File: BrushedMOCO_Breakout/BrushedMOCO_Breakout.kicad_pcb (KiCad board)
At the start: 2 copper layers, 39.9 x 46.2 mm, 30 parts, among them Q1 Si4156DY, Q2 Si4156DY, Q3 Si4156DY, Q4 Si4156DY, U1 74LVC2G04, U2 IRS2308, U3 IRS2308

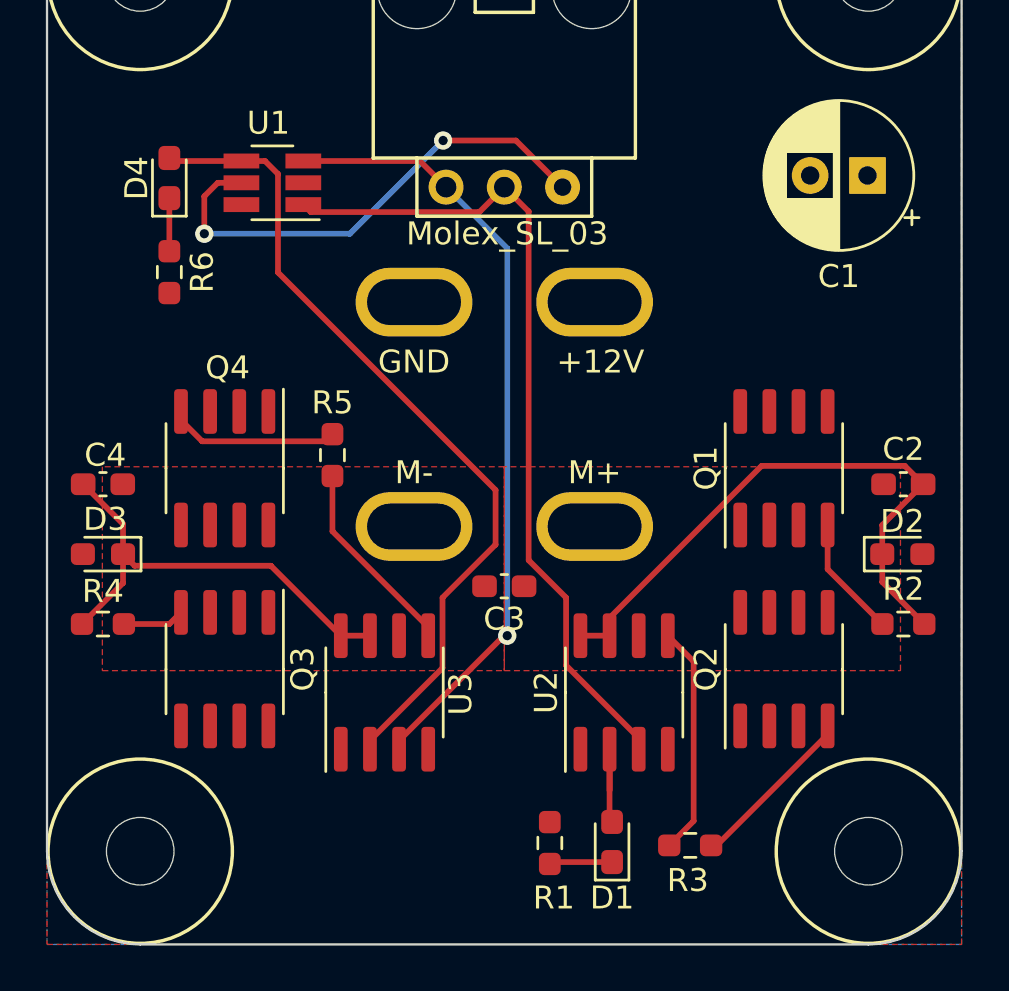
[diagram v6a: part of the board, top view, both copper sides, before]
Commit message: Adjustments
Fixed track width, moved Q2,Q3 further from the mounting holes, reduced vertical space between Andersons, moved some labels
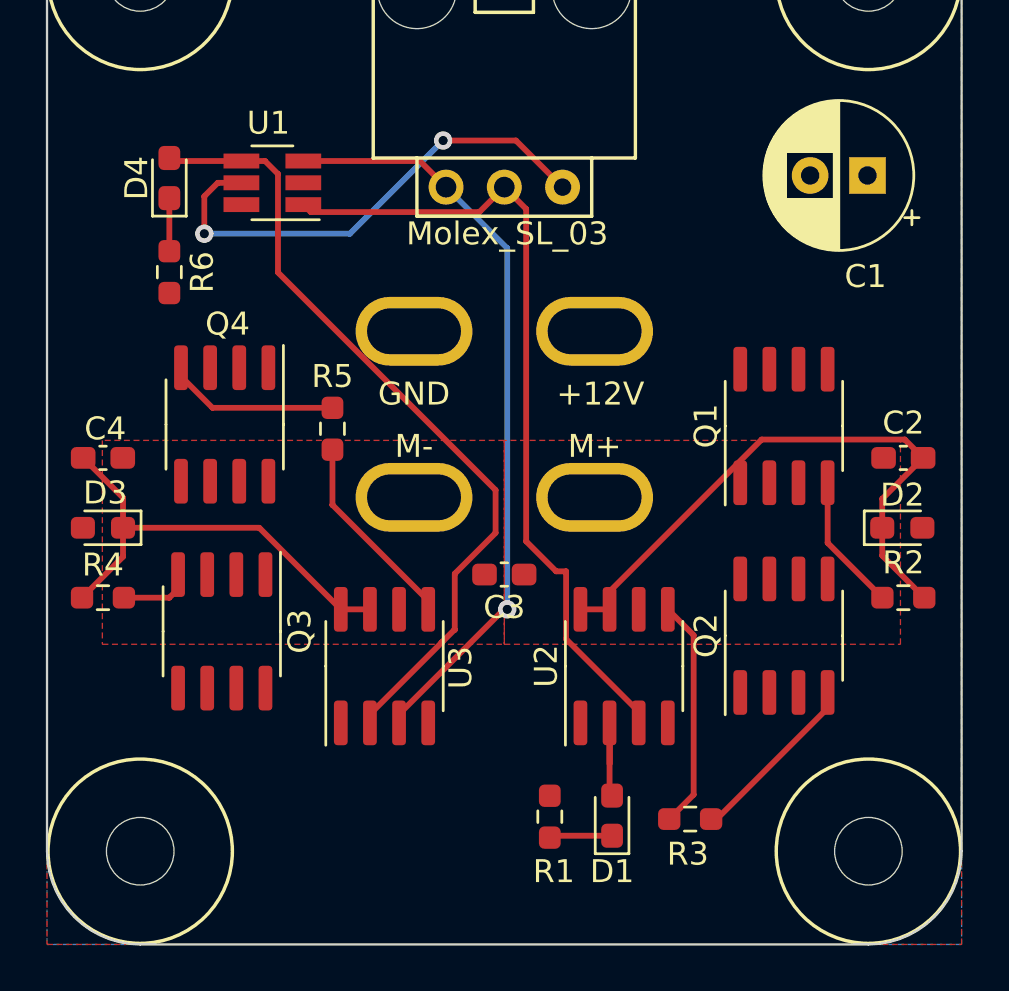
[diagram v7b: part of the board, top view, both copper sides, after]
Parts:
- moved G*** 30.0 mm to (132.3, 86.4), turned to 90 degrees
- moved G*** 7.17 mm to (132.0, 111.8), turned to 90 degrees
- moved Q4 1.91 mm to (109.3, 99.8)
- moved Q1 1.84 mm to (133.7, 99.8)
- moved Q3 1.65 mm to (109.2, 108.8)
- moved Q2 1.46 mm to (133.7, 109.0)
- moved Conn1 1.27 mm to (117.1, 96.1)
- moved Conn2 1.27 mm to (126.0, 102.6)
- moved D1 1.15 mm to (126.2, 116.8)
- moved R1 1.15 mm to (123.5, 116.9)
- moved U2 1.15 mm to (126.8, 110.3)
- moved U3 1.15 mm to (116.3, 110.3)
- moved C2 1.15 mm to (138.9, 101.2)
- moved C4 1.15 mm to (104.0, 101.2)
- moved D2 1.15 mm to (138.9, 104.3)
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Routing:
- net PWM_RVS: track 34.3 -> 33.2 mm
- net Net-(D4-A): track 36.3 -> 35.2 mm
- net PWM_FWD: track 36.3 -> 35.4 mm

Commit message: Finish layout for order
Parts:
- G*** (x2): moved to F.Cu
- R1, R6: value 120 -> 100
- moved D1 38.2 mm to (112.8, 81.0), turned to 180 degrees
- moved R1 34.6 mm to (112.8, 83.9), turned to 180 degrees
- moved G*** 32.4 mm to (103.3, 96.7), turned to -90 degrees
- moved R6 25.2 mm to (130.4, 83.9), turned to 180 degrees
- moved D4 24.8 mm to (130.4, 81.0), turned to 180 degrees
- moved R3 21.0 mm to (136.4, 97.0), turned to 90 degrees
- moved G*** 12.5 mm to (139.8, 96.4)
- moved R4 12.0 mm to (112.9, 115.3), turned to 180 degrees
- moved R2 11.9 mm to (130.2, 115.3), turned to 0 degrees
- moved Q2 10.5 mm to (131.8, 98.6), turned to -90 degrees
- moved Q1 9.65 mm to (131.8, 109.3), turned to -90 degrees
- moved R5 8.04 mm to (106.6, 97.0)
- moved C3 5.21 mm to (121.5, 101.1)
- moved C1 4.78 mm to (132.8, 90.4), turned to 90 degrees
- moved U1 4.34 mm to (107.2, 88.3)
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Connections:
- C1 pad 1: GND -> +12V
- C1 pad 2: +12V -> GND
- D1 pad 2: Net-(D1-A) -> PWM_FWD
- D4 pad 2: Net-(D4-A) -> PWM_RVS
- R2 pad 1: Net-(D2-K) -> Net-(U2-HO)
- R4 pad 1: Net-(D3-K) -> Net-(U3-HO)
- U1 pad 4: Net-(D4-A) -> Net-(U3-LIN)
- U1 pad 6: Net-(D1-A) -> Net-(U2-LIN)
- U2 pad 2: Net-(D1-A) -> PWM_FWD
- U2 pad 3: PWM_FWD -> Net-(U2-LIN)
- U2 pad 7: Net-(D2-K) -> Net-(U2-HO)
- U3 pad 2: Net-(D4-A) -> PWM_RVS
- U3 pad 3: PWM_RVS -> Net-(U3-LIN)
- U3 pad 7: Net-(D3-K) -> Net-(U3-HO)
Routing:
- net Net-(U2-LIN): track 0.00 -> 49.5 mm, vias 0 -> 2
- net PWM_RVS: track 33.2 -> 79.7 mm, vias 1 -> 2
- net Net-(U3-LIN): track 0.00 -> 46.4 mm, vias 0 -> 2
- net Net-(U2-LO): track 10.1 -> 50.2 mm
- net PWM_FWD: track 35.4 -> 70.9 mm, vias 0 -> 3
- net Net-(D4-A): track 35.2 -> 0.00 mm
- net Net-(U3-LO): track 8.69 -> 38.7 mm
- net Net-(Q3-G): track 2.70 -> 19.0 mm
- net +12V: track 0.00 -> 10.3 mm, vias 0 -> 18
- net Net-(U2-HO): track 0.00 -> 9.37 mm
- net Net-(U3-HO): track 0.00 -> 8.93 mm
- net Net-(D2-K): track 26.4 -> 33.3 mm
- net Net-(Q1-G): track 5.31 -> 11.8 mm
- net Net-(D3-K): track 19.8 -> 14.4 mm
- net Net-(Q4-G): track 7.99 -> 2.80 mm
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- added copper zone on F.Cu, net +12V
- added copper zone on B.Cu, net GND
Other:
- board text added: "12V"
- board text added: "Brushed MoCo Breakout, Rev1 Mars Rover Design Team Missouri S&T, 2024 Nikolas Hidayat, Evan McGibney"
- board text added: "FWD"
- board text added: "RVS"
- board text removed: "+12V"
- board text removed: "BrushedMOCO Breakout, Rev1 Mars Rover Design Team Missouri S&T, 2024 Nikolas Hidayat, Evan McGibney"
- board text removed: "Molex_SL_03"
